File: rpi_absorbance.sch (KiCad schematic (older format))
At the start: 18 parts, among them P1 CONN_01X04, U1 LTC2461, U2 RPIABS_CONN, U3 SD100-13-23-222, U4 OPA381

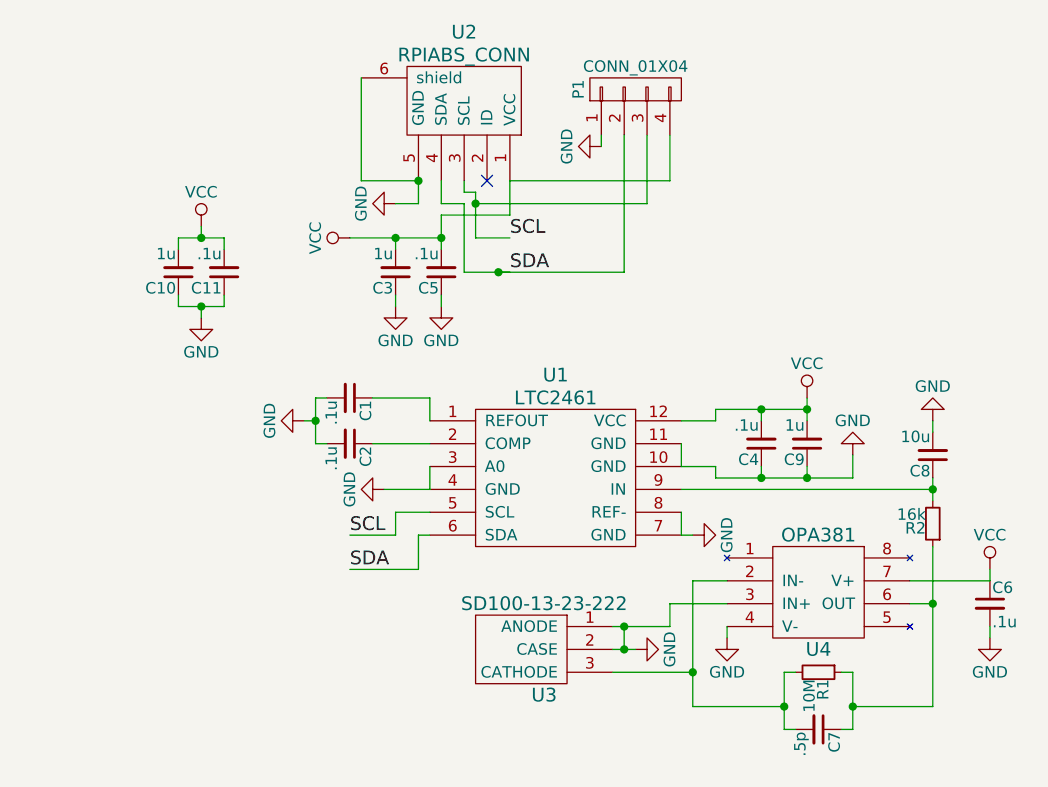
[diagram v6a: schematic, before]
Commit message: Add I2C resistors and reorganize PCB
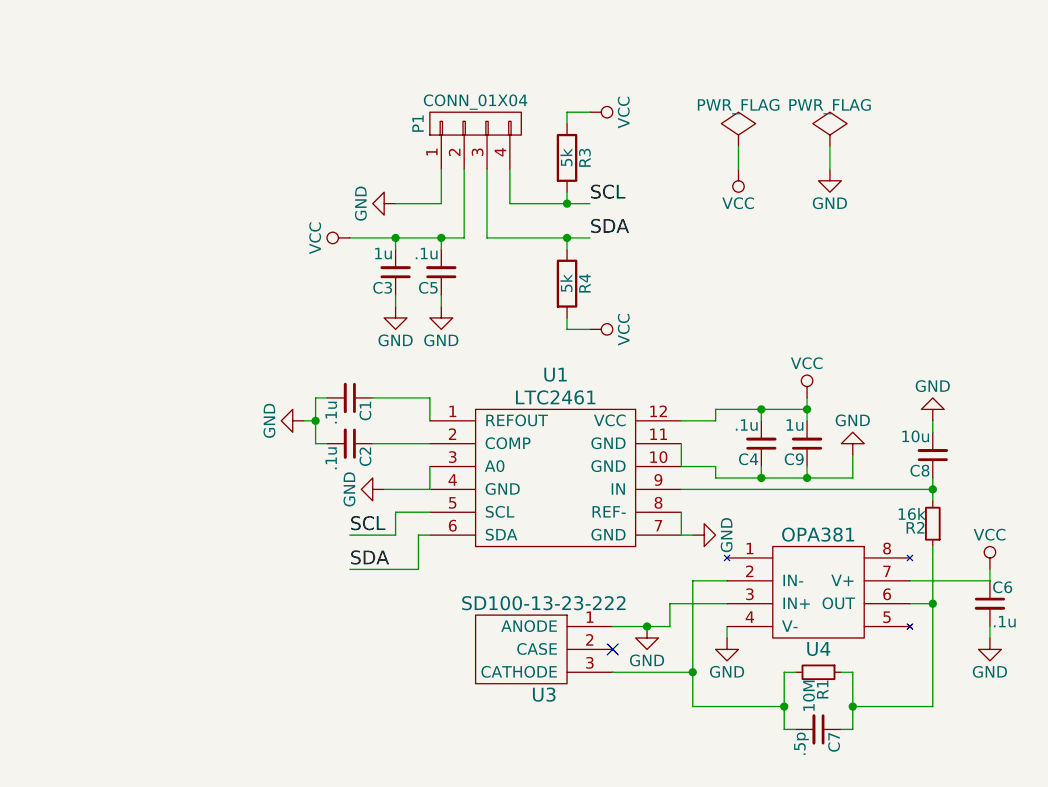
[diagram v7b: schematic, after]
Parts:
- removed C10: 1u, Capacitors_SMD:C_0603, symbol C_Small
- removed C11: .1u, Capacitors_SMD:C_0603, symbol C_Small
- removed U2: RPIABS_CONN, footprints:FCI_10104111-0001LF, symbol RPIABS_CONN
- added R3, R4: 5k, Resistors_SMD:R_0603, symbol R
- P1: footprint footprints:Hirose_DF13-4P-1.25V(20) -> Pin_Headers:Pin_Header_Straight_1x04
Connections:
- net GND: no longer U3.2 (CASE)
- net SCL: now also P1.4 (P4), R3.2; no longer P1.3 (P3)
- net SDA: now also P1.3 (P3), R4.1; no longer P1.2 (P2)
- net VCC: now also P1.2 (P2), R3.1, R4.2; no longer P1.4 (P4)
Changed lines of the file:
@@
 L GND #PWR06
 U 1 1 569AF99E
-P 5450 4550
-F 0 "#PWR06" H 5450 4300 50  0001 C CNN
-F 1 "GND" H 5450 4400 50  0000 C CNN
-F 2 "" H 5450 4550 50  0000 C CNN
-F 3 "" H 5450 4550 50  0000 C CNN
-	1    5450 4550
-	0    -1   -1   0
+P 5500 4450
+F 0 "#PWR06" H 5500 4200 50  0001 C CNN
+F 1 "GND" H 5500 4300 50  0000 C CNN
+F 2 "" H 5500 4450 50  0000 C CNN
+F 3 "" H 5500 4450 50  0000 C CNN
+	1    5500 4450
+	1    0    0    -1
 $EndComp
 $Comp
@@
 Text Label 4200 4050 0    60   ~ 0
 SCL
-Text Label 4900 2900 0    60   ~ 0
-SDA
-Text Label 4900 2750 0    60   ~ 0
-SCL
-Wire Wire Line
-	4500 2500 4500 2600
-Wire Wire Line
-	4500 2600 4400 2600
+Wire Wire Line
+	4400 2600 4600 2600
 Wire Wire Line
 	4550 3850 4550 3750
 Wire Wire Line
 	4350 3850 4550 3850
-Wire Wire Line
-	4750 2750 4900 2750
-Wire Wire Line
-	4700 2900 4900 2900
 Wire Wire Line
 	4500 4200 4200 4200
@@
 Wire Wire Line
 	5850 4500 5850 4450
-Connection ~ 5400 4450
-Wire Wire Line
-	5400 4450 5400 4550
+Connection ~ 5500 4450
 Wire Wire Line
 	5350 4450 5600 4450
@@
 Wire Wire Line
 	5350 4650 5700 4650
-Connection ~ 5400 4550
-Wire Wire Line
-	5350 4550 5450 4550
 Wire Wire Line
 	6750 4350 6650 4350
@@
 Wire Wire Line
 	7000 4250 7000 4200
+Wire Wire Line
+	4200 2750 4700 2750
+Wire Wire Line
+	4400 2750 4400 2800
+Wire Wire Line
+	4400 3000 4400 3050
+Wire Wire Line
+	4600 3050 4600 3000
+NoConn ~ 5350 4550
+$Comp
+L CONN_01X04 P1
+U 1 1 56AD2071
+P 4750 2250
+F 0 "P1" H 4750 2500 50  0000 C CNN
+F 1 "CONN_01X04" V 4850 2250 50  0000 C CNN
+F 2 "Pin_Headers:Pin_Header_Straight_1x04" H 4750 2250 50  0001 C CNN
+F 3 "" H 4750 2250 50  0000 C CNN
+	1    4750 2250
+	0    -1   -1   0
+$EndComp
+Wire Wire Line
+	4600 2600 4600 2450
+Wire Wire Line
+	4700 2750 4700 2450
+Wire Wire Line
+	4600 2800 4600 2750
 Connection ~ 4600 2750
 Wire Wire Line
-	4200 2750 4600 2750
-Wire Wire Line
-	4400 2800 4400 2750
-Wire Wire Line
-	4400 3000 4400 3050
-Wire Wire Line
-	4600 3050 4600 3000
-$Comp
-L RPIABS_CONN U2
-U 1 1 56A00864
-P 4700 1950
-F 0 "U2" H 4700 2050 60  0000 C CNN
-F 1 "RPIABS_CONN" H 4700 1950 60  0000 C CNN
-F 2 "footprints:FCI_10104111-0001LF" H 4700 1950 60  0001 C CNN
-F 3 "" H 4700 1950 60  0000 C CNN
-	1    4700 1950
-	1    0    0    -1
-$EndComp
-Wire Wire Line
-	4250 2050 4250 2500
-Wire Wire Line
-	4900 2500 5600 2500
-$Comp
-L GND #PWR015
-U 1 1 56A00F92
-P 5300 2350
-F 0 "#PWR015" H 5300 2100 50  0001 C CNN
-F 1 "GND" H 5300 2200 50  0000 C CNN
-F 2 "" H 5300 2350 50  0000 C CNN
-F 3 "" H 5300 2350 50  0000 C CNN
-	1    5300 2350
-	0    1    1    0
-$EndComp
-Wire Wire Line
-	5300 2350 5300 2300
-$Comp
-L CONN_01X04 P1
-U 1 1 56A52DAF
-P 5450 2100
-F 0 "P1" H 5450 2350 50  0000 C CNN
-F 1 "CONN_01X04" V 5550 2100 50  0000 C CNN
-F 2 "footprints:Hirose_DF13-4P-1.25V(20)" H 5450 2100 50  0001 C CNN
-F 3 "" H 5450 2100 50  0000 C CNN
-	1    5450 2100
-	0    -1   -1   0
-$EndComp
-Wire Wire Line
-	4700 2900 4700 2600
-Wire Wire Line
-	4700 2600 4600 2600
-Wire Wire Line
-	4600 2600 4600 2500
-Wire Wire Line
-	4750 2750 4750 2550
-Wire Wire Line
-	4750 2550 4700 2550
-Wire Wire Line
-	4700 2550 4700 2500
-Wire Wire Line
-	4600 2650 4600 2800
-Wire Wire Line
-	4600 2650 4900 2650
-Wire Wire Line
-	4900 2650 4900 2500
-Connection ~ 4500 2500
-$Comp
-L C_Small C10
-U 1 1 56A55EED
-P 3450 2900
-F 0 "C10" H 3460 2970 50  0000 L CNN
-F 1 "1u" H 3460 2820 50  0000 L CNN
-F 2 "Capacitors_SMD:C_0603" H 3450 2900 50  0001 C CNN
-F 3 "" H 3450 2900 50  0000 C CNN
-	1    3450 2900
-	-1   0    0    1
-$EndComp
-$Comp
-L C_Small C11
-U 1 1 56A55F64
-P 3650 2900
-F 0 "C11" H 3660 2970 50  0000 L CNN
-F 1 ".1u" H 3660 2820 50  0000 L CNN
-F 2 "Capacitors_SMD:C_0603" H 3650 2900 50  0001 C CNN
-F 3 "" H 3650 2900 50  0000 C CNN
-	1    3650 2900
-	-1   0    0    1
-$EndComp
-Wire Wire Line
-	3450 2800 3450 2750
-Wire Wire Line
-	3450 2750 3650 2750
-Wire Wire Line
-	3650 2750 3650 2800
-$Comp
-L VCC #PWR016
-U 1 1 56A56088
-P 3550 2700
-F 0 "#PWR016" H 3550 2550 50  0001 C CNN
-F 1 "VCC" H 3550 2850 50  0000 C CNN
-F 2 "" H 3550 2700 50  0000 C CNN
-F 3 "" H 3550 2700 50  0000 C CNN
-	1    3550 2700
-	1    0    0    -1
-$EndComp
-Wire Wire Line
-	3550 2700 3550 2750
-Connection ~ 3550 2750
-Wire Wire Line
-	3450 3000 3450 3050
-Wire Wire Line
-	3450 3050 3650 3050
-Wire Wire Line
-	3650 3050 3650 3000
-$Comp
-L GND #PWR017
-U 1 1 56A561B1
-P 3550 3100
-F 0 "#PWR017" H 3550 2850 50  0001 C CNN
-F 1 "GND" H 3550 2950 50  0000 C CNN
-F 2 "" H 3550 3100 50  0000 C CNN
-F 3 "" H 3550 3100 50  0000 C CNN
-	1    3550 3100
-	1    0    0    -1
-$EndComp
-Wire Wire Line
-	3550 3100 3550 3050
-Connection ~ 3550 3050
-Wire Wire Line
-	4250 2500 4500 2500
-NoConn ~ 4800 2500
-Wire Wire Line
-	5600 2500 5600 2300
-Wire Wire Line
-	4750 2600 5500 2600
-Wire Wire Line
-	5500 2600 5500 2300
-Connection ~ 4750 2600
-Wire Wire Line
-	4850 2900 5400 2900
-Wire Wire Line
-	5400 2900 5400 2300
-Connection ~ 4850 2900
+	4800 2450 4800 2750
+Wire Wire Line
+	4800 2750 5250 2750
+Text Label 5250 2750 0    60   ~ 0
+SDA
+Wire Wire Line
+	4900 2450 4900 2600
+Wire Wire Line
+	4900 2600 5250 2600
+Text Label 5250 2600 0    60   ~ 0
+SCL
+$Comp
+L PWR_FLAG #FLG015
+U 1 1 56AD25FD
+P 5900 2350
+F 0 "#FLG015" H 5900 2445 50  0001 C CNN
+F 1 "PWR_FLAG" H 5900 2530 50  0000 C CNN
+F 2 "" H 5900 2350 50  0000 C CNN
+F 3 "" H 5900 2350 50  0000 C CNN
+	1    5900 2350
+	1    0    0    -1
+$EndComp
+$Comp
+L PWR_FLAG #FLG016
+U 1 1 56AD2653
+P 6300 2350
+F 0 "#FLG016" H 6300 2445 50  0001 C CNN
+F 1 "PWR_FLAG" H 6300 2530 50  0000 C CNN
+F 2 "" H 6300 2350 50  0000 C CNN
+F 3 "" H 6300 2350 50  0000 C CNN
+	1    6300 2350
+	1    0    0    -1
+$EndComp
+$Comp
+L VCC #PWR017
+U 1 1 56AD2682
+P 5900 2450
+F 0 "#PWR017" H 5900 2300 50  0001 C CNN
+F 1 "VCC" H 5900 2600 50  0000 C CNN
+F 2 "" H 5900 2450 50  0000 C CNN
+F 3 "" H 5900 2450 50  0000 C CNN
+	1    5900 2450
+	-1   0    0    1
+$EndComp
+Wire Wire Line
+	5900 2350 5900 2450
+$Comp
+L GND #PWR018
+U 1 1 56AD2722
+P 6300 2450
+F 0 "#PWR018" H 6300 2200 50  0001 C CNN
+F 1 "GND" H 6300 2300 50  0000 C CNN
+F 2 "" H 6300 2450 50  0000 C CNN
+F 3 "" H 6300 2450 50  0000 C CNN
+	1    6300 2450
+	1    0    0    -1
+$EndComp
+Wire Wire Line
+	6300 2450 6300 2350
+$Comp
+L R R3
+U 1 1 56AD38FC
+P 5150 2400
+F 0 "R3" V 5230 2400 50  0000 C CNN
+F 1 "5k" V 5150 2400 50  0000 C CNN
+F 2 "Resistors_SMD:R_0603" V 5080 2400 50  0001 C CNN
+F 3 "" H 5150 2400 50  0000 C CNN
+	1    5150 2400
+	1    0    0    -1
+$EndComp
+$Comp
+L R R4
+U 1 1 56AD3947
+P 5150 2950
+F 0 "R4" V 5230 2950 50  0000 C CNN
+F 1 "5k" V 5150 2950 50  0000 C CNN
+F 2 "Resistors_SMD:R_0603" V 5080 2950 50  0001 C CNN
+F 3 "" H 5150 2950 50  0000 C CNN
+	1    5150 2950
+	1    0    0    -1
+$EndComp
+$Comp
+L VCC #PWR019
+U 1 1 56AD3A0C
+P 5250 2200
+F 0 "#PWR019" H 5250 2050 50  0001 C CNN
+F 1 "VCC" H 5250 2350 50  0000 C CNN
+F 2 "" H 5250 2200 50  0000 C CNN
+F 3 "" H 5250 2200 50  0000 C CNN
+	1    5250 2200
+	0    1    1    0
+$EndComp
+$Comp
+L VCC #PWR020
+U 1 1 56AD3A4A
+P 5250 3150
+F 0 "#PWR020" H 5250 3000 50  0001 C CNN
+F 1 "VCC" H 5250 3300 50  0000 C CNN
+F 2 "" H 5250 3150 50  0000 C CNN
+F 3 "" H 5250 3150 50  0000 C CNN
+	1    5250 3150
+	0    1    1    0
+$EndComp
+Wire Wire Line
+	5150 2250 5150 2200
+Wire Wire Line
+	5150 2200 5250 2200
+Wire Wire Line
+	5150 3100 5150 3150
+Wire Wire Line
+	5150 3150 5250 3150
+Wire Wire Line
+	5150 2800 5150 2750
+Connection ~ 5150 2750
+Wire Wire Line
+	5150 2550 5150 2600
+Connection ~ 5150 2600
 $EndSCHEMATC

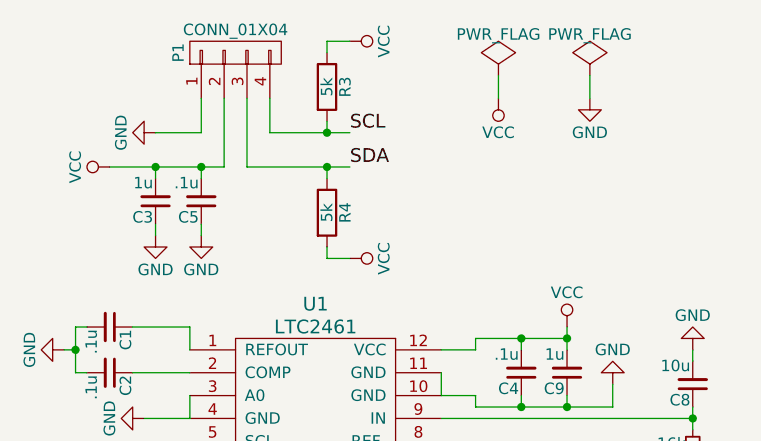
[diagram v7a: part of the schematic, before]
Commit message: Change footprints
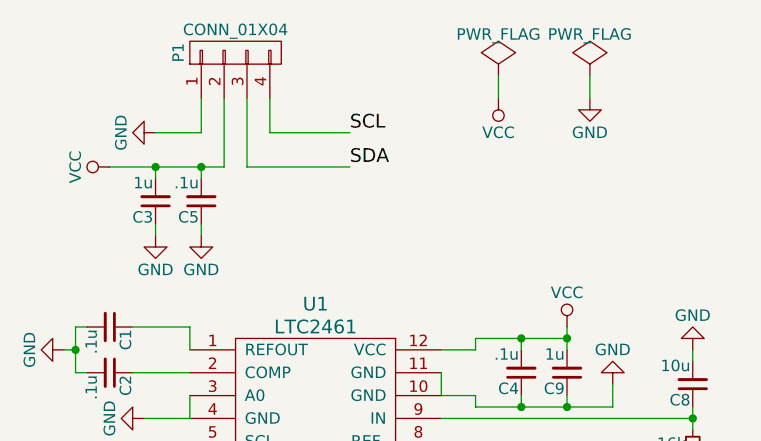
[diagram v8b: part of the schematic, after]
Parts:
- removed R3, R4: 5k, Resistors_SMD:R_0603, symbol R
- R1, R2: footprint Resistors_SMD:R_0603 -> footprints:R_0603_smaller_handsolder
- U3: footprint footprints:TO-5 -> footprints:SD100-13-23-222
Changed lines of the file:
@@
 F 0 "U3" H 5050 3850 60  0000 C CNN
 F 1 "SD100-13-23-222" H 5050 4250 60  0000 C CNN
-F 2 "footprints:TO-5" H 5100 4300 60  0001 C CNN
+F 2 "footprints:SD100-13-23-222" H 5100 4300 60  0001 C CNN
 F 3 "" H 5100 4300 60  0000 C CNN
 	1    5100 4300
@@
 F 0 "R1" H 6280 4670 50  0000 L CNN
 F 1 "10M" H 6280 4610 50  0000 L CNN
-F 2 "Resistors_SMD:R_0603" H 6250 4650 50  0001 C CNN
+F 2 "footprints:R_0603_smaller_handsolder" H 6250 4650 50  0001 C CNN
 F 3 "" H 6250 4650 50  0000 C CNN
 	1    6250 4650
@@
 F 0 "R2" H 6780 4020 50  0000 L CNN
 F 1 "16k" H 6780 3960 50  0000 L CNN
-F 2 "Resistors_SMD:R_0603" H 6750 4000 50  0001 C CNN
+F 2 "footprints:R_0603_smaller_handsolder" H 6750 4000 50  0001 C CNN
 F 3 "" H 6750 4000 50  0000 C CNN
 	1    6750 4000
@@
 Wire Wire Line
 	6300 2450 6300 2350
-$Comp
-L R R3
-U 1 1 56AD38FC
-P 5150 2400
-F 0 "R3" V 5230 2400 50  0000 C CNN
-F 1 "5k" V 5150 2400 50  0000 C CNN
-F 2 "Resistors_SMD:R_0603" V 5080 2400 50  0001 C CNN
-F 3 "" H 5150 2400 50  0000 C CNN
-	1    5150 2400
-	1    0    0    -1
-$EndComp
-$Comp
-L R R4
-U 1 1 56AD3947
-P 5150 2950
-F 0 "R4" V 5230 2950 50  0000 C CNN
-F 1 "5k" V 5150 2950 50  0000 C CNN
-F 2 "Resistors_SMD:R_0603" V 5080 2950 50  0001 C CNN
-F 3 "" H 5150 2950 50  0000 C CNN
-	1    5150 2950
-	1    0    0    -1
-$EndComp
-$Comp
-L VCC #PWR019
-U 1 1 56AD3A0C
-P 5250 2200
-F 0 "#PWR019" H 5250 2050 50  0001 C CNN
-F 1 "VCC" H 5250 2350 50  0000 C CNN
-F 2 "" H 5250 2200 50  0000 C CNN
-F 3 "" H 5250 2200 50  0000 C CNN
-	1    5250 2200
-	0    1    1    0
-$EndComp
-$Comp
-L VCC #PWR020
-U 1 1 56AD3A4A
-P 5250 3150
-F 0 "#PWR020" H 5250 3000 50  0001 C CNN
-F 1 "VCC" H 5250 3300 50  0000 C CNN
-F 2 "" H 5250 3150 50  0000 C CNN
-F 3 "" H 5250 3150 50  0000 C CNN
-	1    5250 3150
-	0    1    1    0
-$EndComp
-Wire Wire Line
-	5150 2250 5150 2200
-Wire Wire Line
-	5150 2200 5250 2200
-Wire Wire Line
-	5150 3100 5150 3150
-Wire Wire Line
-	5150 3150 5250 3150
-Wire Wire Line
-	5150 2800 5150 2750
-Connection ~ 5150 2750
-Wire Wire Line
-	5150 2550 5150 2600
-Connection ~ 5150 2600
 $EndSCHEMATC
